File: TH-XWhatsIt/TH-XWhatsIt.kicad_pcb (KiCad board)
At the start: 2 copper layers, 145.3 x 129.6 mm, 32 parts, among them J1 MODEL F, J2 EXPANSION, J3 EXPANSION HEADER, J4 EXPANSION BEAMSPRING, J5 BEAMSPRING CONNECTOR, J6 EXPANSION BEAMSPRING, J7 EXPANSION DISPLAYWRITER, J8 DISPLAYWRITER CONNECTOR, J9 EXPANSION DISPLAYWRITER, U1 MCP4921-EP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

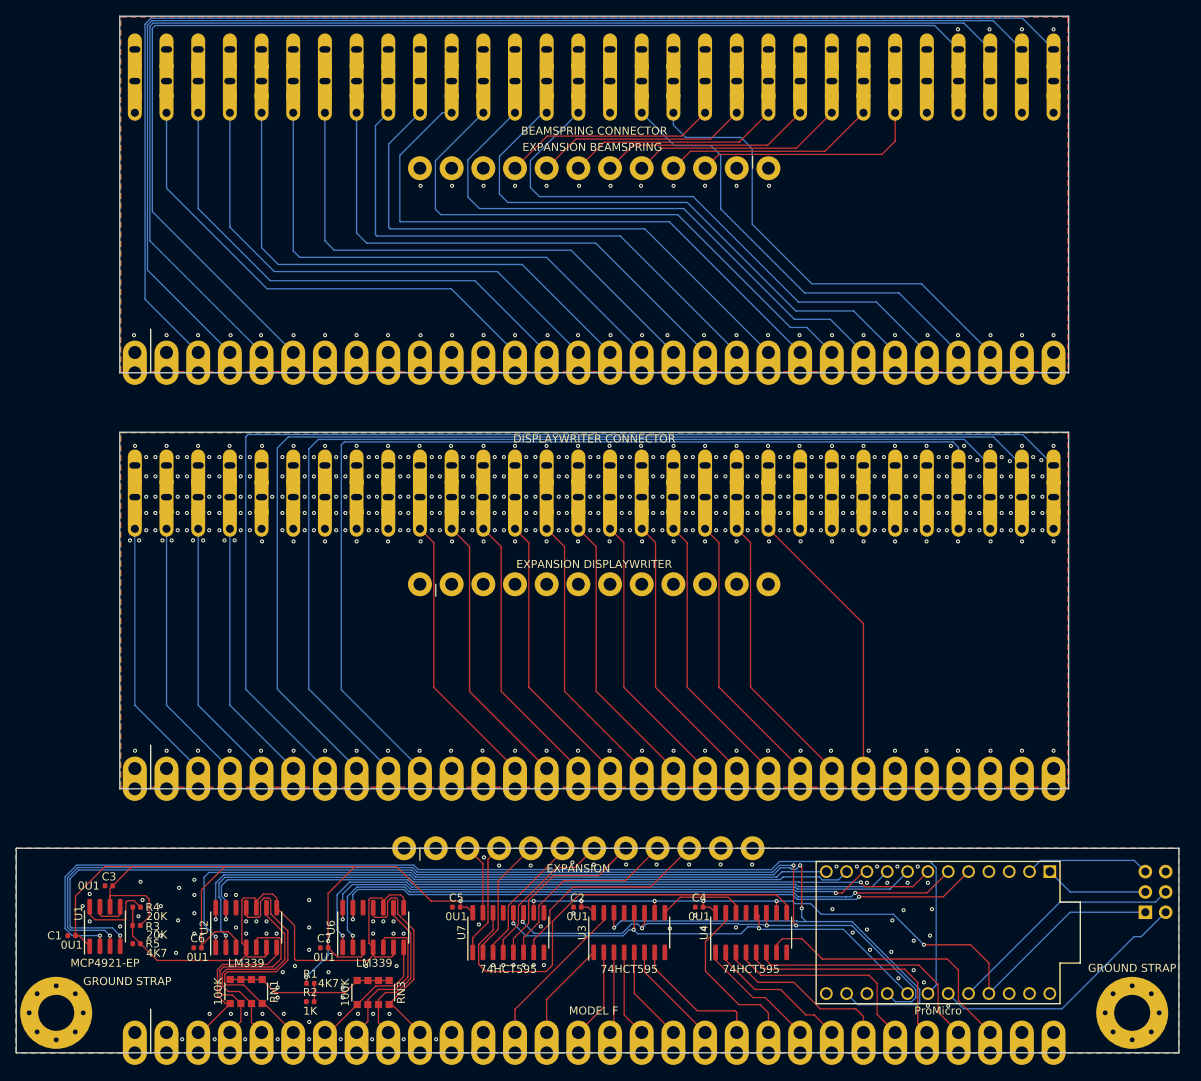
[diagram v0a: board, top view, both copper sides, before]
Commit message: pcb: fix castellation alignment issues
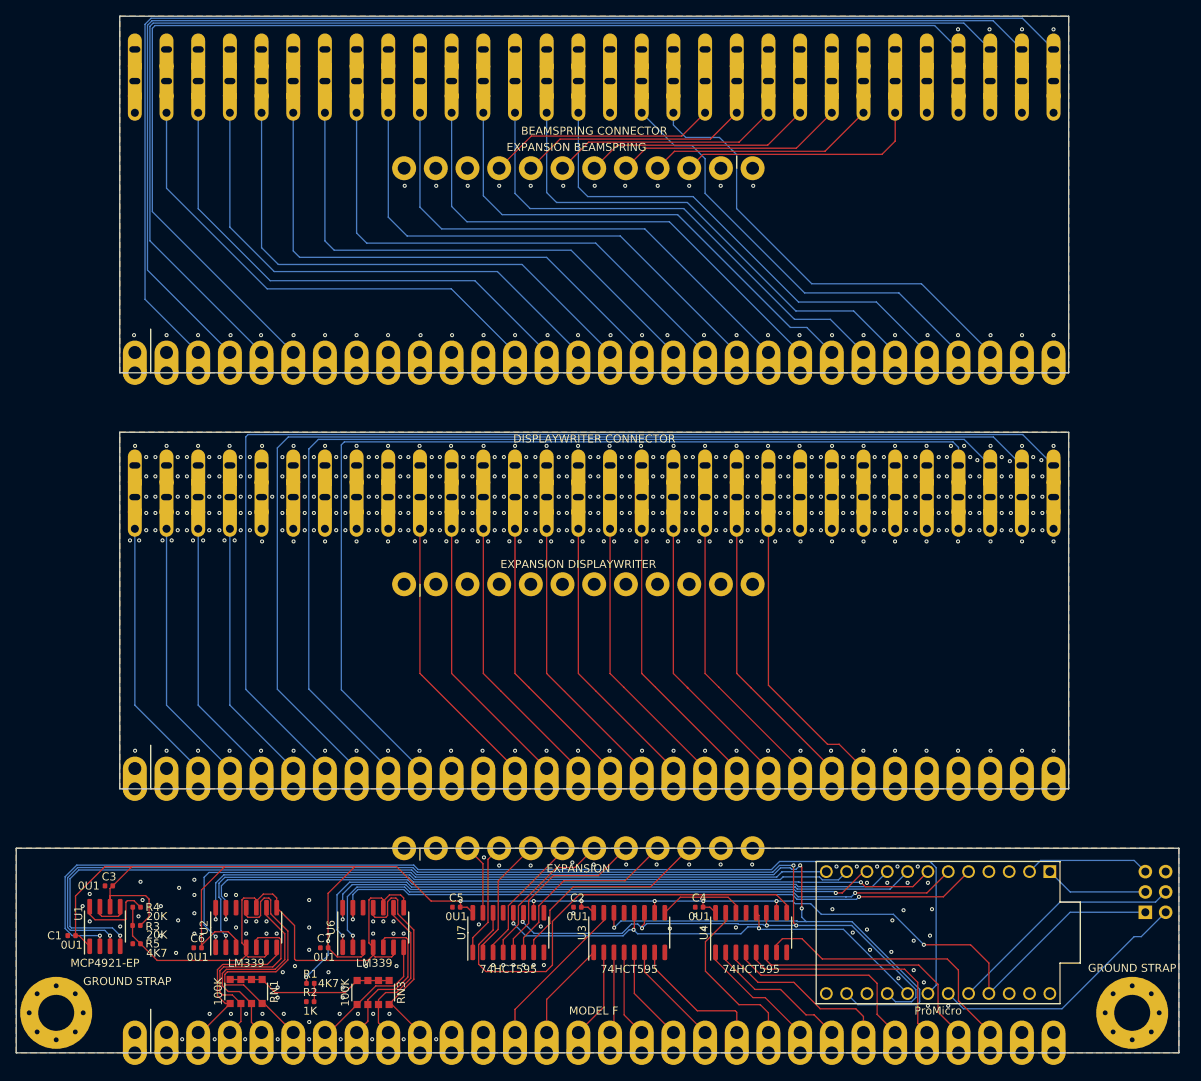
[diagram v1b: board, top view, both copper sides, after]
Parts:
- moved J6 1.98 mm to (101.0, 43.4)
- moved J9 1.98 mm to (101.0, 95.4)
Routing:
- net /beamspring plugboard/BSCOL10: track 81.7 -> 70.8 mm
- net /beamspring plugboard/BSCOL11: track 79.4 -> 70.0 mm
- net /beamspring plugboard/BSCOL12: track 78.4 -> 69.8 mm
- net /beamspring plugboard/BSCOL14: track 77.8 -> 69.3 mm
- net /beamspring plugboard/BSCOL13: track 78.5 -> 70.2 mm
- net /beamspring plugboard/BSCOL9: track 77.8 -> 70.8 mm
- net /beamspring plugboard/BSCOL8: track 75.1 -> 71.5 mm
- net /beamspring plugboard/BSCOL23: track 36.6 -> 38.6 mm
- net /beamspring plugboard/BSCOL22: track 34.6 -> 36.5 mm
- net /beamspring plugboard/BSCOL20: track 34.6 -> 36.5 mm
- net /beamspring plugboard/BSCOL17: track 34.6 -> 36.5 mm
- net /beamspring plugboard/BSCOL18: track 34.6 -> 36.5 mm
- net /beamspring plugboard/BSCOL21: track 34.6 -> 36.5 mm
- net /beamspring plugboard/BSCOL19: track 34.6 -> 36.5 mm
- net /beamspring plugboard/BSCOL16: track 66.4 -> 64.8 mm
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
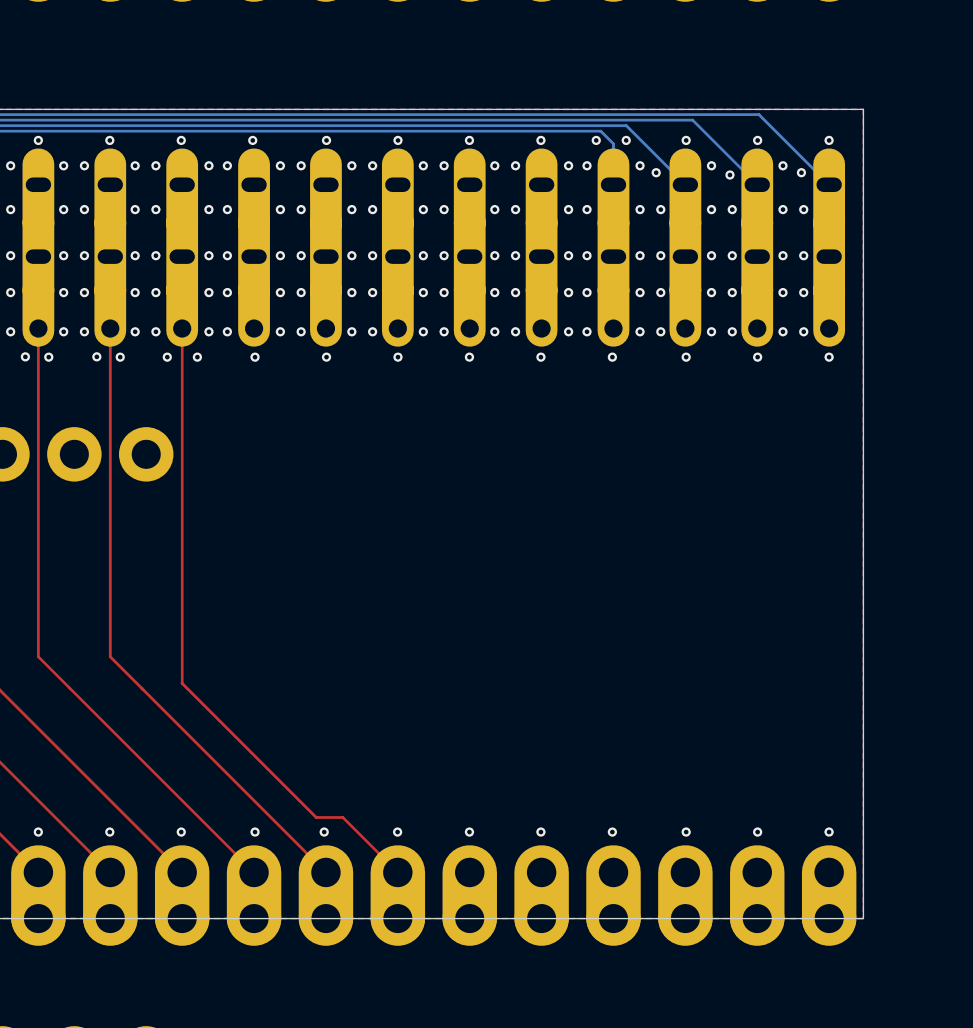
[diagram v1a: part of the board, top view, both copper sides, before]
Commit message: pcb: added cutout to displaywriter
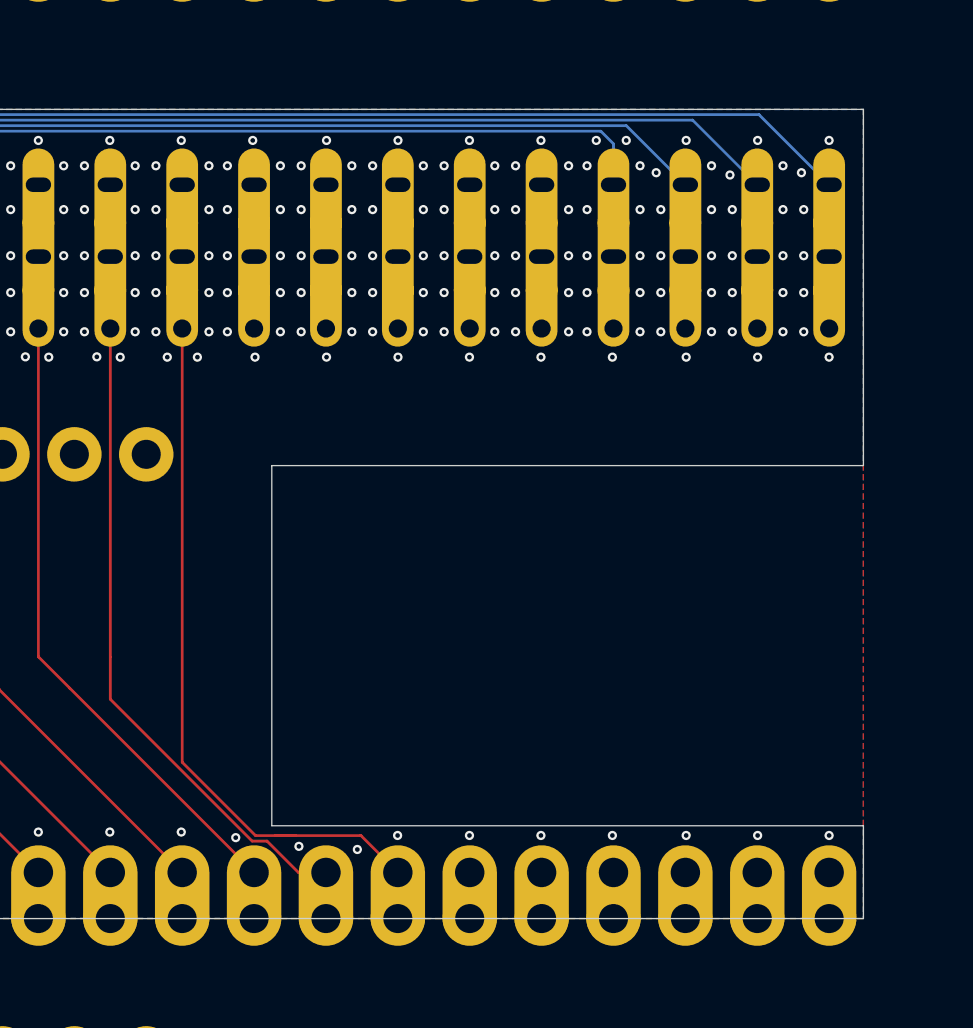
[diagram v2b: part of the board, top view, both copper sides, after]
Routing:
- net /displaywriter plugboard/DWCOL12: track 43.7 -> 47.3 mm
- net /displaywriter plugboard/DWCOL11: track 42.9 -> 45.3 mm
- net /displaywriter plugboard/DWGROUND: vias 393 -> 394
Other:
- outline, holes or cut-outs redrawn
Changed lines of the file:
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@@
   (general
     (thickness 1.6)
-    (drawings 23)
-    (tracks 1398)
+    (drawings 27)
+    (tracks 1404)
     (zones 0)
     (modules 32)
@@
   (layers
     (0 F.Cu signal)
-    (31 B.Cu signal hide)
+    (31 B.Cu signal)
     (32 B.Adhes user hide)
     (33 F.Adhes user hide)
@@
     )
   )
+  (gr_line (start 129.653 96.018) (end 129.653 115.858) (layer Edge.Cuts) (width 0.05))
+  (gr_line (start 162.246 76.394) (end 162.246 96.018) (layer Edge.Cuts) (width 0.05))
+  (gr_line (start 162.246 120.971) (end 162.246 115.858) (layer Edge.Cuts) (width 0.05))
+  (gr_line (start 129.653 115.858) (end 162.246 115.858) (layer Edge.Cuts) (width 0.05))
+  (gr_line (start 129.653 96.018) (end 162.246 96.018) (layer Edge.Cuts) (width 0.05))
   (dimension 129.58 (width 0.12) (layer Dwgs.User)
     (gr_text "129.580 mm" (at 196.342 89.181 90) (layer Dwgs.User)
@@
   )
   (gr_line (start 43.628 120.971) (end 162.246 120.971) (layer Edge.Cuts) (width 0.05))
-  (gr_line (start 162.246 120.971) (end 162.246 76.394) (layer Edge.Cuts) (width 0.05))
   (gr_line (start 43.628 76.394) (end 162.246 76.394) (layer Edge.Cuts) (width 0.05))
   (gr_line (start 43.628 120.971) (end 43.628 76.394) (layer Edge.Cuts) (width 0.05))
@@
   (segment (start 47.705 25.908) (end 47.705 48.816) (width 0.1524) (layer B.Cu) (net 77))
   (segment (start 145.49204 25.55904) (end 48.05396 25.55904) (width 0.1524) (layer B.Cu) (net 77))
-  (via (at 160.354 116.205) (size 0.508) (drill 0.254) (layers F.Cu B.Cu) (net 78))
-  (via (at 148.416 116.205) (size 0.508) (drill 0.254) (layers F.Cu B.Cu) (net 78))
-  (via (at 144.479 116.205) (size 0.508) (drill 0.254) (layers F.Cu B.Cu) (net 78))
-  (via (at 140.542 116.205) (size 0.508) (drill 0.254) (layers F.Cu B.Cu) (net 78))
+  (via (at 160.354 116.39296) (size 0.508) (drill 0.254) (layers F.Cu B.Cu) (net 78))
+  (via (at 148.416 116.39296) (size 0.508) (drill 0.254) (layers F.Cu B.Cu) (net 78))
+  (via (at 144.479 116.39296) (size 0.508) (drill 0.254) (layers F.Cu B.Cu) (net 78))
+  (via (at 140.542 116.39296) (size 0.508) (drill 0.254) (layers F.Cu B.Cu) (net 78))
   (via (at 99.521 86.487) (size 0.508) (drill 0.254) (layers F.Cu B.Cu) (net 78))
   (via (at 151.083 86.487) (size 0.508) (drill 0.254) (layers F.Cu B.Cu) (net 78))
@@
   (via (at 155.02 86.487) (size 0.508) (drill 0.254) (layers F.Cu B.Cu) (net 78))
   (via (at 141.939 86.487) (size 0.508) (drill 0.254) (layers F.Cu B.Cu) (net 78))
-  (via (at 156.417 116.205) (size 0.508) (drill 0.254) (layers F.Cu B.Cu) (net 78))
-  (via (at 152.48 116.205) (size 0.508) (drill 0.254) (layers F.Cu B.Cu) (net 78))
+  (via (at 156.417 116.39296) (size 0.508) (drill 0.254) (layers F.Cu B.Cu) (net 78))
+  (via (at 152.48 116.39296) (size 0.508) (drill 0.254) (layers F.Cu B.Cu) (net 78))
   (via (at 54.817 79.502) (size 0.508) (drill 0.254) (layers F.Cu B.Cu) (net 78))
   (via (at 103.458 79.502) (size 0.508) (drill 0.254) (layers F.Cu B.Cu) (net 78))
@@
   (via (at 153.877 84.455) (size 0.508) (drill 0.254) (layers F.Cu B.Cu) (net 78))
   (via (at 151.083 84.455) (size 0.508) (drill 0.254) (layers F.Cu B.Cu) (net 78))
-  (via (at 132.541 116.205) (size 0.508) (drill 0.254) (layers F.Cu B.Cu) (net 78))
-  (via (at 128.731 116.205) (size 0.508) (drill 0.254) (layers F.Cu B.Cu) (net 78))
-  (via (at 136.58342 116.205) (size 0.508) (drill 0.254) (layers F.Cu B.Cu) (net 78))
+  (via (at 131.14782 116.9924) (size 0.508) (drill 0.254) (layers F.Cu B.Cu) (net 78))
+  (via (at 127.66802 116.51234) (size 0.508) (drill 0.254) (layers F.Cu B.Cu) (net 78))
+  (via (at 136.58342 116.39296) (size 0.508) (drill 0.254) (layers F.Cu B.Cu) (net 78))
   (via (at 112.856 116.205) (size 0.508) (drill 0.254) (layers F.Cu B.Cu) (net 78))
   (via (at 108.919 116.205) (size 0.508) (drill 0.254) (layers F.Cu B.Cu) (net 78))
@@
   (via (at 84.45626 90.02776) (size 0.508) (drill 0.254) (layers F.Cu B.Cu) (net 78))
   (via (at 123.89612 90.043) (size 0.508) (drill 0.254) (layers F.Cu B.Cu) (net 78))
+  (via (at 134.366 117.16512) (size 0.508) (drill 0.254) (layers F.Cu B.Cu) (net 78))
   (segment (start 124.717 80.547) (end 124.717 88.467) (width 0.1524) (layer F.Cu) (net 79) (status 30))
-  (segment (start 124.717 108.0165) (end 132.10286 115.40236) (width 0.1524) (layer F.Cu) (net 79))
-  (segment (start 124.717 88.467) (end 124.717 108.0165) (width 0.1524) (layer F.Cu) (net 79))
-  (segment (start 133.56836 115.40236) (end 136.597 118.431) (width 0.1524) (layer F.Cu) (net 79))
-  (segment (start 132.10286 115.40236) (end 133.56836 115.40236) (width 0.1524) (layer F.Cu) (net 79))
+  (segment (start 136.597 118.431) (end 134.56358 116.39758) (width 0.1524) (layer F.Cu) (net 79))
+  (segment (start 128.75722 116.39758) (end 130.9527 116.39758) (width 0.1524) (layer F.Cu) (net 79))
+  (segment (start 124.717 112.35736) (end 128.75722 116.39758) (width 0.1524) (layer F.Cu) (net 79))
+  (segment (start 124.717 88.467) (end 124.717 112.35736) (width 0.1524) (layer F.Cu) (net 79))
+  (segment (start 130.9527 116.39758) (end 129.833922 116.39758) (width 0.1524) (layer F.Cu) (net 79))
+  (segment (start 134.56358 116.39758) (end 130.9527 116.39758) (width 0.1524) (layer F.Cu) (net 79))
   (segment (start 120.757 80.547) (end 120.757 88.467) (width 0.1524) (layer F.Cu) (net 80) (status 30))
-  (segment (start 120.757 106.551) (end 122.5587 108.3527) (width 0.1524) (layer F.Cu) (net 80))
-  (segment (start 120.757 88.467) (end 120.757 106.551) (width 0.1524) (layer F.Cu) (net 80))
-  (segment (start 122.5587 108.3527) (end 132.637 118.431) (width 0.1524) (layer F.Cu) (net 80))
-  (segment (start 122.485601 108.279601) (end 122.5587 108.3527) (width 0.1524) (layer F.Cu) (net 80))
+  (segment (start 132.637 118.431) (end 131.48329 118.431) (width 0.1524) (layer F.Cu) (net 80))
+  (segment (start 120.757 106.551) (end 120.757 88.467) (width 0.1524) (layer F.Cu) (net 80))
+  (segment (start 120.757 108.88707) (end 120.757 106.551) (width 0.1524) (layer F.Cu) (net 80))
+  (segment (start 128.57232 116.70239) (end 120.757 108.88707) (width 0.1524) (layer F.Cu) (net 80))
+  (segment (start 129.393013 116.70239) (end 128.57232 116.70239) (width 0.1524) (layer F.Cu) (net 80))
+  (segment (start 131.121623 118.431) (end 129.393013 116.70239) (width 0.1524) (layer F.Cu) (net 80))
+  (segment (start 132.637 118.431) (end 131.121623 118.431) (width 0.1524) (layer F.Cu) (net 80))
   (segment (start 118.525601 108.279601) (end 128.677 118.431) (width 0.1524) (layer F.Cu) (net 81) (status 20))
   (segment (start 116.797 80.547) (end 116.797 88.467) (width 0.1524) (layer F.Cu) (net 81) (status 30))
